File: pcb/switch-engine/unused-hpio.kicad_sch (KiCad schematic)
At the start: 1 part, among them U8 XILINX_ULTRASCALEPLUS_B676

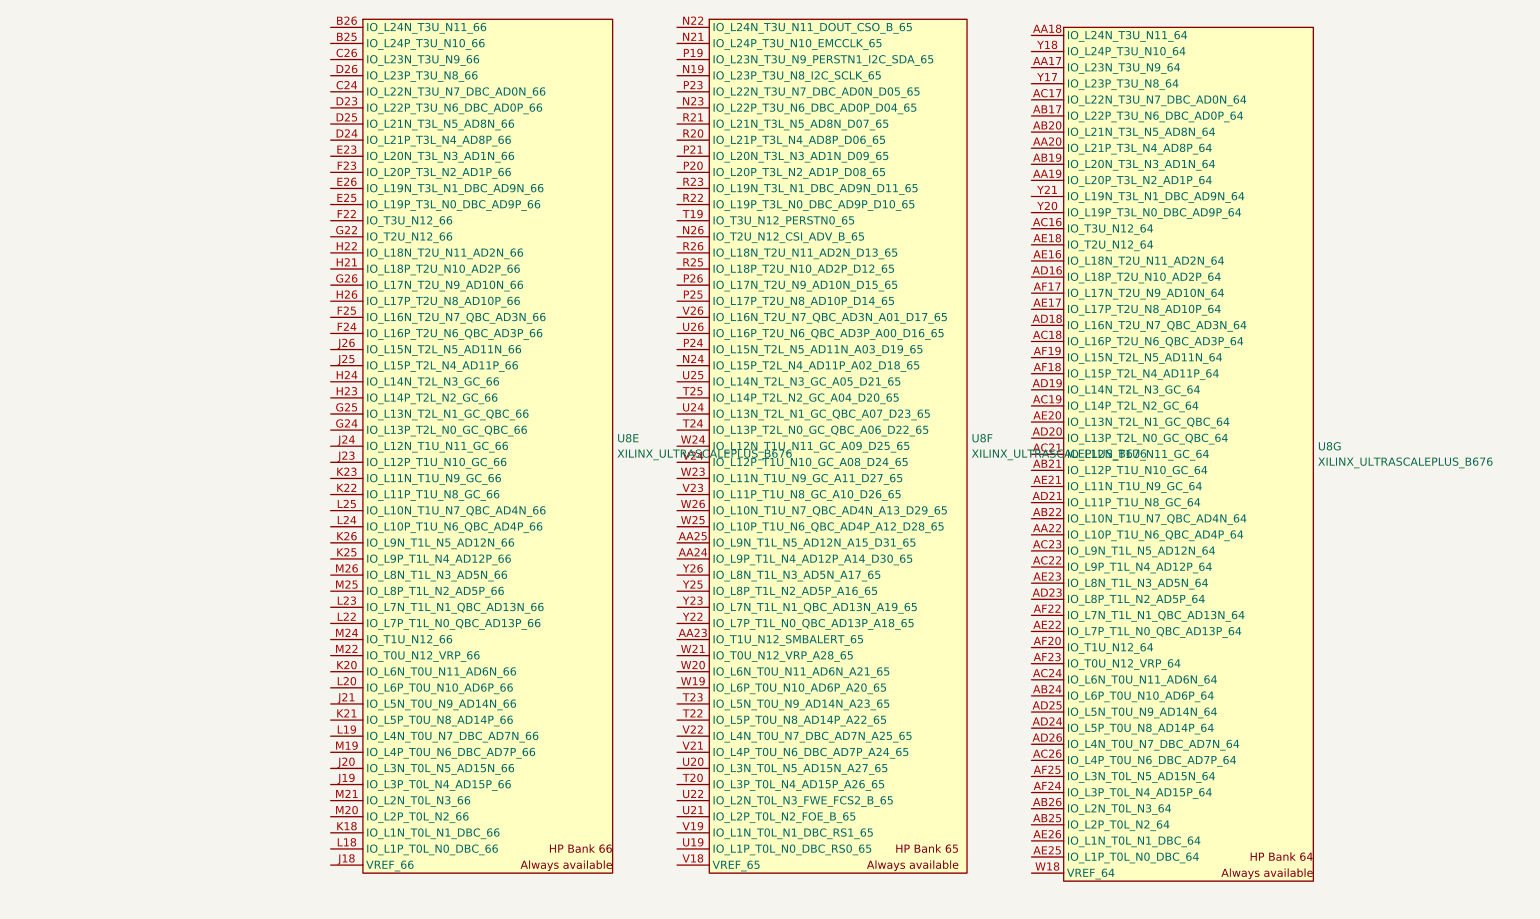
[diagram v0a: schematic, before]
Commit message: First iteration of main board PCB schematic is now passing ERC
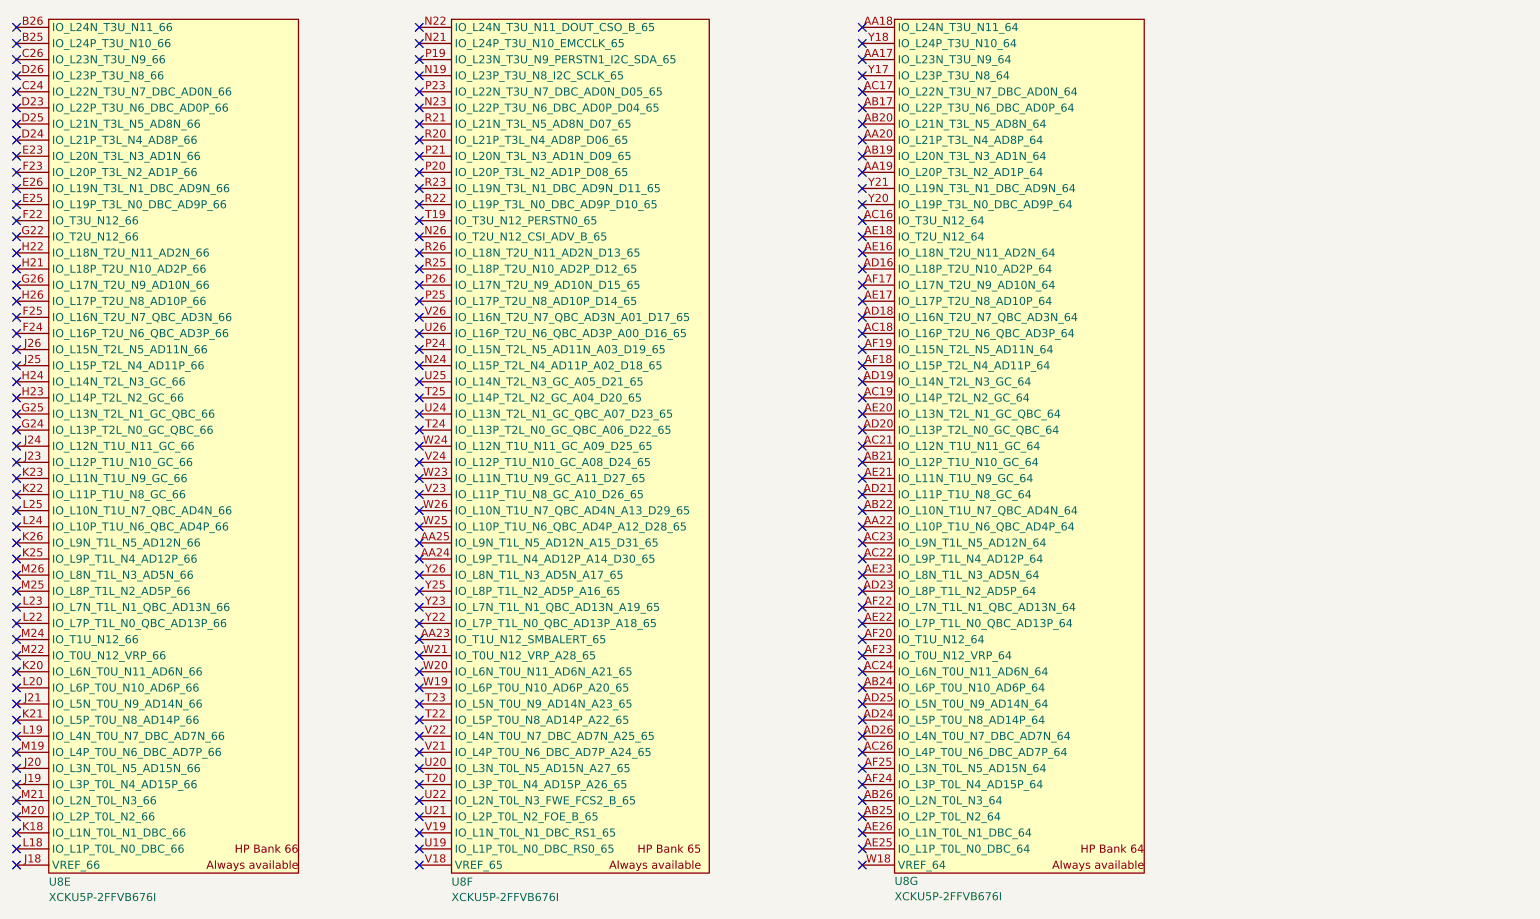
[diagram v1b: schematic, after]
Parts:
- U8: value XILINX_ULTRASCALEPLUS_B676 -> XCKU5P-2FFVB676I
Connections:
- no-connect marks 0 -> 159
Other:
- company: (none) -> Antikernel Labs
- title: (none) -> LATENTRED Ethernet Switch - Main Board
- moved on the sheet: U8E, U8F, U8G

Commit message: Added footprints and created initial skeleton of layout
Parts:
- U8: footprint (none) -> azonenberg_pcb:BGA_676_27x27_FULLARRAY_1MM_FFG676
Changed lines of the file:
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@@
 			)
 		)
-		(property "Footprint" ""
+		(property "Footprint" "azonenberg_pcb:BGA_676_27x27_FULLARRAY_1MM_FFG676"
 			(at 240.03 156.21 0)
 			(effects
@@
 			)
 		)
-		(property "Footprint" ""
+		(property "Footprint" "azonenberg_pcb:BGA_676_27x27_FULLARRAY_1MM_FFG676"
 			(at 170.18 156.21 0)
 			(effects
@@
 			)
 		)
-		(property "Footprint" ""
+		(property "Footprint" "azonenberg_pcb:BGA_676_27x27_FULLARRAY_1MM_FFG676"
 			(at 106.68 156.21 0)
 			(effects
